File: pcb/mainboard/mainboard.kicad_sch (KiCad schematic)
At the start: 0 parts

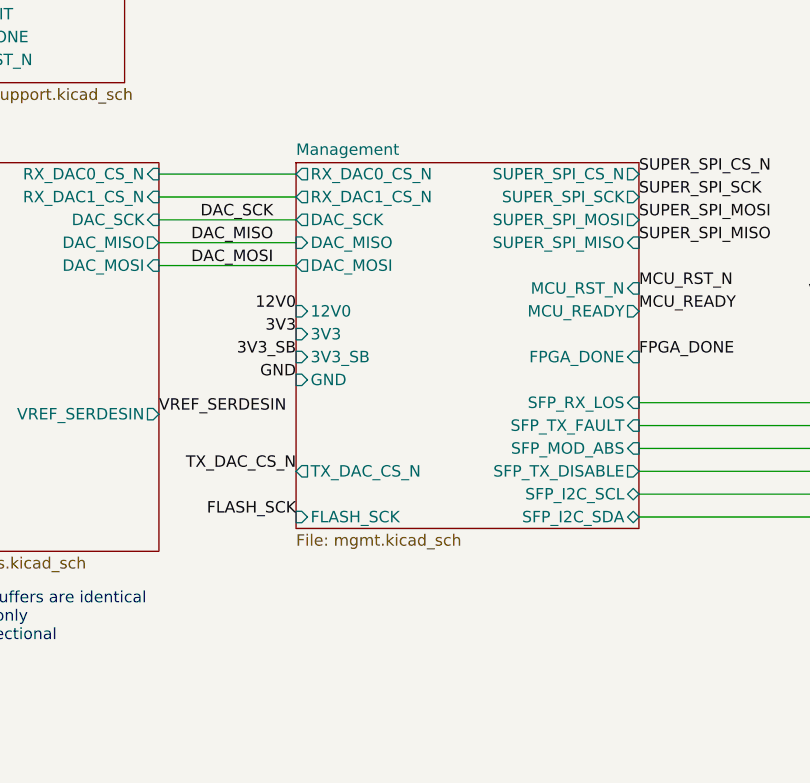
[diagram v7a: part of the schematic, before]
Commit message: Finished initial schematic review of trigger crossbar mainboard
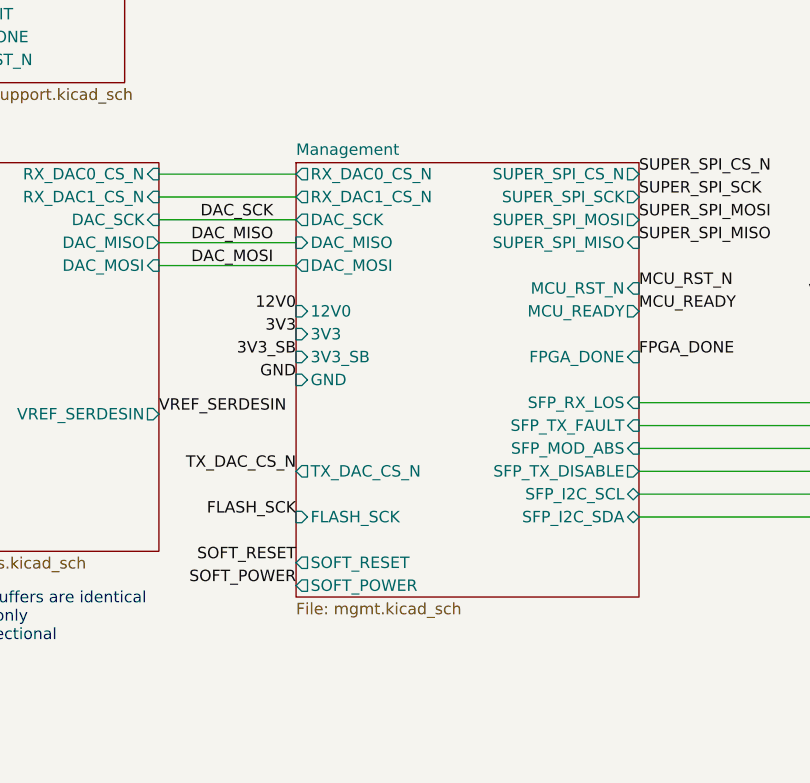
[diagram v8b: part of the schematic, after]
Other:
- sheet Management ports: added SOFT_POWER, SOFT_RESET; removed none
